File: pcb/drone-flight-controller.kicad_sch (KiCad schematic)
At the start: 88 parts, among them J1 SWD, J10 CONN_MANDO, J11 OLED, J12 STM32 SPI, J13 STM32 I2C, J14 STM32 USART, J2 Jumper, J3 USB_B_Micro, J4 CONN_MOT_1, J5 CONN_MOT_2, J6 CONN_MOT_3, J7 CONN_MOT_4, J8 XT-60, J9 LIDAR, SW1 TS24CA_C393942, SW2 TS24CA_C393942, SW4 SW_Push_SPDT, U1 STM32F103R8T6, U10 LM7805_TO220, U11 AMS1117-3.3, U2 MPU-6050, Y1 8MHz, Y2 32.768KHz

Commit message: pcb: switch SW1-SW3 to the TC-6610 THT tact switch (C7528713)
Replace the low-profile side-actuated TS24CA with a tall 9mm 6x6 THT
button that stays reachable on the assembled frame. The 4-pin part has
internally shorted pin pairs across its 6.5mm axis, so the distinct
1/2/3/4 pad numbering of the converted EasyEDA footprint would strap
each net across a shorted pair (STM32 held in reset); use KiCad's
official SW_PUSH_6mm_H9.5mm instead, whose paired 1,1,2,2 pads encode
the topology and drop onto the existing 2-pin symbols. Headless KiCad
10 ERC is identical before and after.
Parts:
- SW1, SW2: value TS24CA_C393942 -> TC-6610_C7528713; footprint easyeda:SW-SMD_2P-TS24CA -> Button_Switch_THT:SW_PUSH_6mm_H9.5mm; LCSC C393942 -> C7528713; Manufacturer SHOU HAN -> FG; Part TS24CA -> TC-6610 -6*6*9-260g
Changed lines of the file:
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@@
 			)
 		)
-		(property "Value" "TS24CA_C393942"
+		(property "Value" "TC-6610_C7528713"
 			(at 385.064 162.56 90)
 			(hide yes)
@@
 			)
 		)
-		(property "Footprint" "easyeda:SW-SMD_2P-TS24CA"
+		(property "Footprint" "Button_Switch_THT:SW_PUSH_6mm_H9.5mm"
 			(at 387.35 161.29 0)
 			(hide yes)
@@
 			)
 		)
-		(property "Datasheet" "https://www.lcsc.com/datasheet/lcsc_datasheet_2404241539_SHOU-HAN-TS24CA_C393942.pdf"
+		(property "Datasheet" "https://wmsc.lcsc.com/wmsc/upload/file/pdf/v2/lcsc/2401191746_FG-TC-6610--6-6-9-260g_C7528713.pdf"
 			(at 387.35 161.29 0)
 			(hide yes)
@@
 			)
 		)
-		(property "Description" "Push button switch, generic, two pins"
+		(property "Description" "-20℃~+70℃ 12V 2.6N 50,000 cycles 50mA 6mm 6mm Black Round Button SPST Through Hole Without Bracket 插件-4P,6x6mm Tactile Switches ROHS"
 			(at 382.27 161.29 0)
 			(hide yes)
@@
 			)
 		)
-		(property "LCSC" "C393942"
+		(property "LCSC" "C7528713"
 			(at 382.27 161.29 0)
 			(hide yes)
@@
 			)
 		)
-		(property "Part" "TS24CA"
+		(property "Part" "TC-6610 -6*6*9-260g"
 			(at 382.27 161.29 0)
 			(hide yes)
@@
 			)
 		)
-		(property "Manufacturer" "SHOU HAN"
+		(property "Manufacturer" "FG"
 			(at 382.27 161.29 0)
 			(hide yes)
@@
 			)
 		)
-		(property "Value" "TS24CA_C393942"
+		(property "Value" "TC-6610_C7528713"
 			(at 25.4 199.3899 90)
 			(hide yes)
@@
 			)
 		)
-		(property "Footprint" "easyeda:SW-SMD_2P-TS24CA"
+		(property "Footprint" "Button_Switch_THT:SW_PUSH_6mm_H9.5mm"
 			(at 26.67 198.12 0)
 			(hide yes)
@@
 			)
 		)
-		(property "Datasheet" "https://www.lcsc.com/datasheet/lcsc_datasheet_2404241539_SHOU-HAN-TS24CA_C393942.pdf"
+		(property "Datasheet" "https://wmsc.lcsc.com/wmsc/upload/file/pdf/v2/lcsc/2401191746_FG-TC-6610--6-6-9-260g_C7528713.pdf"
 			(at 26.67 198.12 0)
 			(hide yes)
@@
 			)
 		)
-		(property "Description" "Push button switch, generic, two pins"
+		(property "Description" "-20℃~+70℃ 12V 2.6N 50,000 cycles 50mA 6mm 6mm Black Round Button SPST Through Hole Without Bracket 插件-4P,6x6mm Tactile Switches ROHS"
 			(at 21.59 198.12 0)
 			(hide yes)
@@
 			)
 		)
-		(property "LCSC" "C393942"
+		(property "LCSC" "C7528713"
 			(at 21.59 198.12 0)
 			(hide yes)
@@
 			)
 		)
-		(property "Part" "TS24CA"
+		(property "Part" "TC-6610 -6*6*9-260g"
 			(at 21.59 198.12 0)
 			(hide yes)
@@
 			)
 		)
-		(property "Manufacturer" "SHOU HAN"
+		(property "Manufacturer" "FG"
 			(at 21.59 198.12 0)
 			(hide yes)

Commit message: pcb: 3D models for U3, U5, J3, J16
U3 and U5 move from the model-less DigiKey footprints to the official
KiCad TQFP-32 and SOIC-8 footprints, whose STEP models ship with the
AppImage. J3/J16's micro-USB footprint had no model, no MPN, and
unknown provenance - replaced wholesale with the SHOU HAN MicroXNJ
(C404969): converted footprint with shell legs renumbered to the
Shield pin 6, STEP model, and BOM fields, verified against its
datasheet drawing. ERC caught that the LM358 is multi-unit and the
first edit only touched U5A's footprint field; U5B fixed to match.
Headless KiCad 10 ERC identical to baseline.
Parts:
- J3: footprint easyeda:MICRO-USB-SMD_5P-P0.65-H-F_MICRO5.9MMUSB -> easyeda:MICRO-USB-SMD_MICROXNJ_1; LCSC (none) -> C404969; Manufacturer (none) -> SHOU HAN; Part (none) -> MicroXNJ
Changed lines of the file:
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@@
 			)
 		)
-		(property "Footprint" "easyeda:MICRO-USB-SMD_5P-P0.65-H-F_MICRO5.9MMUSB"
+		(property "Footprint" "easyeda:MICRO-USB-SMD_MICROXNJ_1"
 			(at 106.68 267.97 0)
 			(hide yes)
@@
 			)
 		)
-		(property "Datasheet" ""
+		(property "Datasheet" "https://www.lcsc.com/datasheet/lcsc_datasheet_2204151400_SHOU-HAN-MicroXNJ_C404969.pdf"
 			(at 106.68 267.97 0)
 			(hide yes)
@@
 			)
 		)
-		(property "Description" "USB Micro Type B connector"
+		(property "Description" "-20℃~+85℃ 1 1.8A 30V 5,000 times 5P Black Female Micro-B Surface Mount, Right Angle USB 2.0 SMD USB Connectors ROHS"
 			(at 110.49 269.24 0)
 			(hide yes)
@@
 			)
 		)
+    (property "LCSC" "C404969" (at 110.49 269.24 0)
+      (effects (font (size 1.27 1.27)) (hide yes))
+    )
+    (property "Part" "MicroXNJ" (at 110.49 269.24 0)
+      (effects (font (size 1.27 1.27)) (hide yes))
+    )
+    (property "Manufacturer" "SHOU HAN" (at 110.49 269.24 0)
+      (effects (font (size 1.27 1.27)) (hide yes))
+    )
 		(pin "3"
 		)

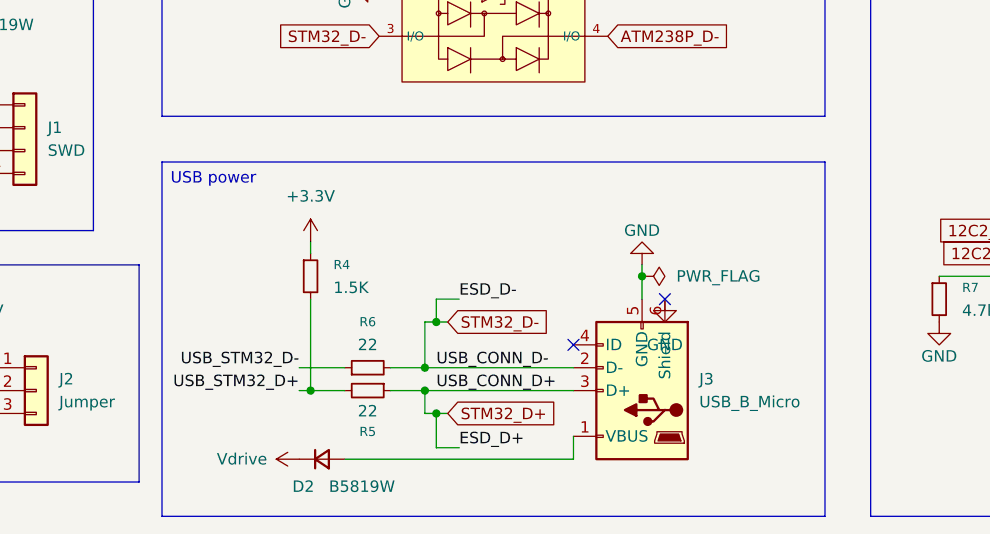
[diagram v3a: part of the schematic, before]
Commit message: pcb: import the new U3/U5/USB footprints onto the board
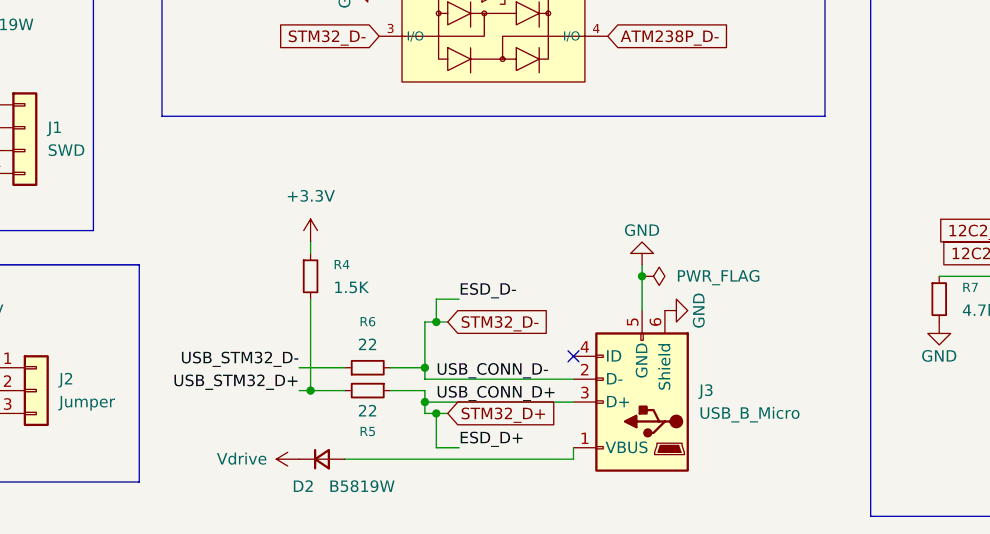
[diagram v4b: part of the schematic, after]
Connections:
- no-connect marks 22 -> 21
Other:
- moved on the sheet: J3
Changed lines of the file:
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@@
 		)
 	)
-	(text_box "USB power\n"
-		(exclude_from_sim no)
-		(at 57.15 243.84 0)
-		(size 73.66 39.37)
-		(margins 0.9525 0.9525 0.9525 0.9525)
-		(stroke
-			(width 0)
-			(type solid)
-		)
-		(fill
-			(type none)
-		)
-		(effects
-			(font
-				(size 1.27 1.27)
-			)
-			(justify left top)
-		)
-	)
 	(text_box "Reset button\n"
 		(exclude_from_sim no)
@@
 	)
 	(junction
-		(at 86.36 266.7)
-		(diameter 0)
-		(color 0 0 0 0)
-	)
-	(junction
-		(at 110.49 256.54)
-		(diameter 0)
-		(color 0 0 0 0)
-	)
-	(junction
 		(at 260.35 234.95)
 		(diameter 0)
@@
 	)
 	(junction
+		(at 86.36 266.7)
+		(diameter 0)
+		(color 0 0 0 0)
+	)
+	(junction
 		(at 161.29 170.18)
 		(diameter 0)
@@
 	)
 	(junction
+		(at 86.36 270.51)
+		(diameter 0)
+		(color 0 0 0 0)
+	)
+	(junction
 		(at 48.26 67.31)
 		(diameter 0)
@@
 	)
 	(junction
+		(at 110.49 256.54)
+		(diameter 0)
+		(color 0 0 0 0)
+	)
+	(junction
 		(at 87.63 271.78)
 		(diameter 0)
@@
 		(color 0 0 0 0)
 	)
-	(junction
-		(at 86.36 269.24)
-		(diameter 0)
-		(color 0 0 0 0)
-	)
 	(no_connect
 		(at 219.71 102.87)
@@
 	)
 	(no_connect
-		(at 102.87 264.16)
+		(at 102.87 265.43)
 	)
 	(no_connect
@@
 	)
 	(no_connect
-		(at 113.03 259.08)
-	)
-	(no_connect
 		(at 184.15 118.11)
 	)
@@
 	(wire
 		(pts
-			(xy 86.36 271.78) (xy 86.36 269.24)
+			(xy 86.36 271.78) (xy 86.36 270.51)
 		)
 		(stroke
@@
 	(wire
 		(pts
-			(xy 86.36 269.24) (xy 102.87 269.24)
+			(xy 86.36 270.51) (xy 102.87 270.51)
 		)
 		(stroke
@@
 	(wire
 		(pts
-			(xy 102.87 274.32) (xy 102.87 276.86)
+			(xy 102.87 275.59) (xy 102.87 276.86)
 		)
 		(stroke
@@
 	(wire
 		(pts
-			(xy 86.36 266.7) (xy 102.87 266.7)
+			(xy 86.36 267.97) (xy 102.87 267.97)
 		)
 		(stroke
@@
 	(wire
 		(pts
-			(xy 110.49 256.54) (xy 110.49 259.08)
+			(xy 86.36 270.51) (xy 86.36 269.24)
 		)
 		(stroke
@@
 	(wire
 		(pts
+			(xy 86.36 267.97) (xy 86.36 266.7)
+		)
+		(stroke
+			(width 0)
+			(type default)
+		)
+	)
+	(wire
+		(pts
 			(xy 177.8 21.59) (xy 177.8 24.13)
 		)
@@
 	(wire
 		(pts
+			(xy 110.49 256.54) (xy 110.49 260.35)
+		)
+		(stroke
+			(width 0)
+			(type default)
+		)
+	)
+	(wire
+		(pts
 			(xy 88.9 261.62) (xy 87.63 261.62)
 		)
@@
 	)
 	(label "USB_CONN_D-"
-		(at 87.63 266.7 0)
+		(at 87.63 267.97 0)
 		(effects
 			(font
@@
 	)
 	(label "USB_CONN_D+"
-		(at 87.63 269.24 0)
+		(at 87.63 270.51 0)
 		(effects
 			(font
@@
 	)
 	(symbol
+		(lib_id "PCM_SparkFun-PowerSymbol:GND")
+		(at 113.03 260.35 90)
+		(unit 1)
+		(body_style 1)
+		(exclude_from_sim no)
+		(in_bom yes)
+		(on_board yes)
+		(in_pos_files yes)
+		(dnp no)
+		(fields_autoplaced yes)
+		(property "Reference" "#PWR078"
+			(at 119.38 260.35 0)
+			(hide yes)
+			(show_name no)
+			(do_not_autoplace no)
+			(effects
+				(font
+					(size 1.27 1.27)
+				)
+			)
+		)
+		(property "Value" "GND"
+			(at 116.84 260.35 0)
+			(show_name no)
+			(do_not_autoplace yes)
+			(effects
+				(font
+					(size 1.27 1.27)
+				)
+			)
+		)
+		(property "Footprint" ""
+			(at 113.03 260.35 0)
+			(hide yes)
+			(show_name no)
+			(do_not_autoplace no)
+			(effects
+				(font
+					(size 1.27 1.27)
+				)
+			)
+		)
+		(property "Datasheet" ""
+			(at 113.03 260.35 0)
+			(hide yes)
+			(show_name no)
+			(do_not_autoplace no)
+			(effects
+				(font
+					(size 1.27 1.27)
+				)
+			)
+		)
+		(property "Description" "Power symbol creates a global label with name \"GND\" , ground"
+			(at 121.92 260.35 0)
+			(hide yes)
+			(show_name no)
+			(do_not_autoplace no)
+			(effects
+				(font
+					(size 1.27 1.27)
+				)
+			)
+		)
+		(pin "1"
+		)
+		(instances
+			(project "drone-flight-controller"
+				(path "/2753c1d5-c5b3-42f6-8923-cca974813b6b"
+					(reference "#PWR078")
+					(unit 1)
+				)
+			)
+		)
+	)
+	(symbol
 		(lib_id "Mechanical:MountingHole_Pad")
 		(at 271.78 232.41 0)
@@
 	(symbol
 		(lib_id "Connector:USB_B_Micro")
-		(at 110.49 269.24 180)
+		(at 110.49 270.51 180)
 		(unit 1)
 		(body_style 1)
@@
 		(fields_autoplaced yes)
 		(property "Reference" "J3"
-			(at 116.84 267.9699 0)
+			(at 116.84 269.2399 0)
 			(show_name no)
 			(do_not_autoplace no)
@@
 		)
 		(property "Value" "USB_B_Micro"
-			(at 116.84 270.5099 0)
+			(at 116.84 271.7799 0)
 			(show_name no)
 			(do_not_autoplace no)
@@
 		)
 		(property "Footprint" "easyeda:MICRO-USB-SMD_MICROXNJ_1"
-			(at 106.68 267.97 0)
+			(at 106.68 269.24 0)
 			(hide yes)
 			(show_name no)
@@
 		)
 		(property "Datasheet" "https://www.lcsc.com/datasheet/lcsc_datasheet_2204151400_SHOU-HAN-MicroXNJ_C404969.pdf"
-			(at 106.68 267.97 0)
+			(at 106.68 269.24 0)
 			(hide yes)
 			(show_name no)
@@
 		)
 		(property "Description" "-20℃~+85℃ 1 1.8A 30V 5,000 times 5P Black Female Micro-B Surface Mount, Right Angle USB 2.0 SMD USB Connectors ROHS"
-			(at 110.49 269.24 0)
+			(at 110.49 270.51 0)
+			(hide yes)
+			(show_name no)
+			(do_not_autoplace no)
+			(effects
+				(font
+					(size 1.27 1.27)
+				)
+			)
+		)
+		(property "LCSC" "C404969"
+			(at 110.49 270.51 0)
+			(hide yes)
+			(show_name no)
+			(do_not_autoplace no)
+			(effects
+				(font
+					(size 1.27 1.27)
+				)
+			)
+		)
+		(property "Part" "MicroXNJ"
+			(at 110.49 270.51 0)
+			(hide yes)
+			(show_name no)
+			(do_not_autoplace no)
+			(effects
+				(font
+					(size 1.27 1.27)
+				)
+			)
+		)
+		(property "Manufacturer" "SHOU HAN"
+			(at 110.49 270.51 0)
 			(hide yes)
 			(show_name no)
@@
 			)
 		)
-    (property "LCSC" "C404969" (at 110.49 269.24 0)
-      (effects (font (size 1.27 1.27)) (hide yes))
-    )
-    (property "Part" "MicroXNJ" (at 110.49 269.24 0)
-      (effects (font (size 1.27 1.27)) (hide yes))
-    )
-    (property "Manufacturer" "SHOU HAN" (at 110.49 269.24 0)
-      (effects (font (size 1.27 1.27)) (hide yes))
-    )
 		(pin "3"
 		)
@@
 					(unit 1)
 				)
-			)
-		)
-	)
-	(symbol
-		(lib_id "power:GND")
-		(at 113.03 259.08 0)
-		(unit 1)
-		(body_style 1)
-		(exclude_from_sim no)
-		(in_bom yes)
-		(on_board yes)
-		(in_pos_files yes)
-		(dnp no)
-		(fields_autoplaced yes)
-		(property "Reference" "#PWR0142"
-			(at 113.03 265.43 0)
-			(hide yes)
-			(show_name no)
-			(do_not_autoplace no)
-			(effects
-				(font
-					(size 1.27 1.27)
-				)
-			)
-		)
-		(property "Value" "GND"
-			(at 113.03 264.16 0)
-			(show_name no)
-			(do_not_autoplace no)
-			(effects
-				(font
-					(size 1.27 1.27)
-				)
-			)
-		)
-		(property "Footprint" ""
-			(at 113.03 259.08 0)
-			(hide yes)
-			(show_name no)
-			(do_not_autoplace no)
-			(effects
-				(font
-					(size 1.27 1.27)
-				)
-			)
-		)
-		(property "Datasheet" ""
-			(at 113.03 259.08 0)
-			(hide yes)
-			(show_name no)
-			(do_not_autoplace no)
-			(effects
-				(font
-					(size 1.27 1.27)
-				)
-			)
-		)
-		(property "Description" "Power symbol creates a global label with name GND, ground"
-			(at 113.03 259.08 0)
-			(hide yes)
-			(show_name no)
-			(do_not_autoplace no)
-			(effects
-				(font
-					(size 1.27 1.27)
-				)
-			)
-		)
-		(pin "1"
-		)
-		(instances
-			(project "drone-flight-controller"
-				(path "/2753c1d5-c5b3-42f6-8923-cca974813b6b"
-					(reference "#PWR0142")
-					(unit 1)
-				)

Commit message: pcb: session state - U10 folded on board, pending sch fixes
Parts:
- U10: footprint Package_TO_SOT_THT:TO-220-3_Vertical -> Package_TO_SOT_THT:TO-220-3_Horizontal_TabDown
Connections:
- net +3.3V: now also J9.2 (Pin_2); no longer J9.5 (Pin_5)
- net +5V: now also J14.4 (Pin_4), J9.6 (Pin_6); no longer J14.1 (Pin_1), J9.1 (Pin_1)
- net GND: now also J14.1 (Pin_1), J3.SH (Shield), J9.3 (Pin_3); no longer J14.4 (Pin_4), J3.6 (Shield), J9.4 (Pin_4)
- net ON_OFF_LIDAR: now also J9.1 (Pin_1); no longer J9.6 (Pin_6)
- net USART1_RX: now also J14.3 (Pin_3), J9.4 (Pin_4); no longer J14.2 (Pin_2), J9.3 (Pin_3)
- net USART1_TX: now also J14.2 (Pin_2), J9.5 (Pin_5); no longer J14.3 (Pin_3), J9.2 (Pin_2)
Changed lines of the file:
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@@
 		)
 	)
+	(text_box "Power\n"
+		(exclude_from_sim no)
+		(at 57.15 245.11 0)
+		(size 72.39 39.37)
+		(margins 0.9525 0.9525 0.9525 0.9525)
+		(stroke
+			(width 0)
+			(type solid)
+		)
+		(fill
+			(type none)
+		)
+		(effects
+			(font
+				(size 1.27 1.27)
+			)
+			(justify left top)
+		)
+	)
 	(text_box "Programming\n"
 		(exclude_from_sim no)
@@
 	(wire
 		(pts
-			(xy 313.69 241.3) (xy 325.12 241.3)
-		)
-		(stroke
-			(width 0)
-			(type default)
-		)
-	)
-	(wire
-		(pts
 			(xy 210.82 29.21) (xy 210.82 31.75)
 		)
@@
 	(wire
 		(pts
+			(xy 313.69 241.3) (xy 325.12 241.3)
+		)
+		(stroke
+			(width 0)
+			(type default)
+		)
+	)
+	(wire
+		(pts
 			(xy 187.96 29.21) (xy 187.96 31.75)
 		)
@@
 	(wire
 		(pts
-			(xy 307.34 238.76) (xy 325.12 238.76)
-		)
-		(stroke
-			(width 0)
-			(type default)
-		)
-	)
-	(wire
-		(pts
 			(xy 271.78 234.95) (xy 260.35 234.95)
 		)
@@
 	(wire
 		(pts
+			(xy 307.34 238.76) (xy 325.12 238.76)
+		)
+		(stroke
+			(width 0)
+			(type default)
+		)
+	)
+	(wire
+		(pts
 			(xy 86.36 261.62) (xy 86.36 266.7)
 		)
@@
 			)
 		)
-		(property "Description" "-20℃~+70℃ 12V 2.6N 50,000 cycles 50mA 6mm 6mm Black Round Button SPST Through Hole Without Bracket 插件-4P,6x6mm Tactile Switches ROHS"
+		(property "Description" "Push button switch, generic, two pins"
 			(at 382.27 161.29 0)
 			(hide yes)
@@
 	(symbol
 		(lib_id "Connector_Generic:Conn_01x06")
-		(at 330.2 236.22 0)
+		(at 330.2 238.76 0)
+		(mirror x)
 		(unit 1)
 		(body_style 1)
@@
 		(in_pos_files yes)
 		(dnp no)
-		(fields_autoplaced yes)
 		(property "Reference" "J9"
-			(at 332.74 236.2199 0)
+			(at 332.74 238.7601 0)
 			(show_name no)
 			(do_not_autoplace no)
@@
 		)
 		(property "Value" "LIDAR"
-			(at 332.74 238.7599 0)
+			(at 332.74 236.2201 0)
 			(show_name no)
 			(do_not_autoplace no)
@@
 		)
 		(property "Footprint" "Connector_PinHeader_2.54mm:PinHeader_1x06_P2.54mm_Horizontal"
-			(at 330.2 236.22 0)
+			(at 330.2 238.76 0)
 			(hide yes)
 			(show_name no)
@@
 		)
 		(property "Datasheet" ""
-			(at 330.2 236.22 0)
+			(at 330.2 238.76 0)
 			(hide yes)
 			(show_name no)
@@
 		)
 		(property "Description" "Generic connector, single row, 01x06, script generated (kicad-library-utils/schlib/autogen/connector/)"
-			(at 330.2 236.22 0)
+			(at 330.2 238.76 0)
 			(hide yes)
 			(show_name no)
@@
 			)
 		)
-		(property "Description" "-20℃~+85℃ 1 1.8A 30V 5,000 times 5P Black Female Micro-B Surface Mount, Right Angle USB 2.0 SMD USB Connectors ROHS"
+		(property "Description" "USB Micro Type B connector"
 			(at 110.49 270.51 0)
 			(hide yes)
@@
 		(pin "1"
 		)
-		(pin "6"
+		(pin "SH"
 		)
 		(pin "4"
@@
 			)
 		)
-		(property "Footprint" "Package_TO_SOT_THT:TO-220-3_Vertical"
+		(property "Footprint" "Package_TO_SOT_THT:TO-220-3_Horizontal_TabDown"
 			(at 59.69 61.595 0)
 			(hide yes)
@@
 			)
 		)
-		(property "Description" "-20℃~+70℃ 12V 2.6N 50,000 cycles 50mA 6mm 6mm Black Round Button SPST Through Hole Without Bracket 插件-4P,6x6mm Tactile Switches ROHS"
+		(property "Description" "Push button switch, generic, two pins"
 			(at 21.59 198.12 0)
 			(hide yes)
@@
 	(symbol
 		(lib_id "Connector_Generic:Conn_01x04")
-		(at 350.52 26.67 0)
+		(at 350.52 29.21 0)
+		(mirror x)
 		(unit 1)
 		(body_style 1)
@@
 		(in_pos_files yes)
 		(dnp no)
-		(fields_autoplaced yes)
 		(property "Reference" "J14"
-			(at 353.06 26.6699 0)
+			(at 353.06 29.2101 0)
 			(show_name no)
 			(do_not_autoplace no)
@@
 		)
 		(property "Value" "STM32 USART"
-			(at 353.06 29.2099 0)
+			(at 353.06 26.6701 0)
 			(show_name no)
 			(do_not_autoplace no)
@@
 		)
 		(property "Footprint" "Connector_PinHeader_2.54mm:PinHeader_1x04_P2.54mm_Horizontal"
-			(at 350.52 26.67 0)
+			(at 350.52 29.21 0)
 			(hide yes)
 			(show_name no)
@@
 		)
 		(property "Datasheet" ""
-			(at 350.52 26.67 0)
+			(at 350.52 29.21 0)
 			(hide yes)
 			(show_name no)
@@
 		)
 		(property "Description" "Generic connector, single row, 01x04, script generated (kicad-library-utils/schlib/autogen/connector/)"
-			(at 350.52 26.67 0)
+			(at 350.52 29.21 0)
 			(hide yes)
 			(show_name no)

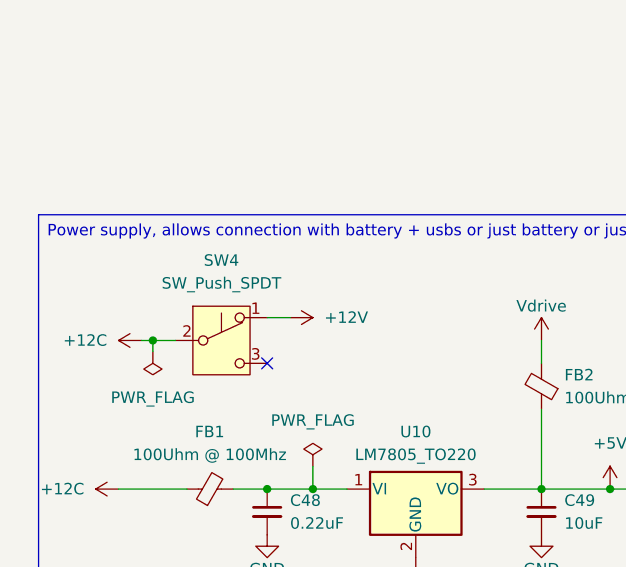
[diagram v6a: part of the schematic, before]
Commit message: pcb: source SW4 as the SS12D10G5 slide switch (C7431054)
Retire the last named unsourced part: the master power switch becomes
a real latching SPDT slide rated 2A/125V - about 5x margin over the
logic tree's draw through the LM7805 branch. The converted footprint's
middle pad is the SPDT common, matching the existing +12V/+12C wiring
with no renumbering, and it brings the 3D model the placeholder
Switch_Slide footprint never had. Headless ERC identical.
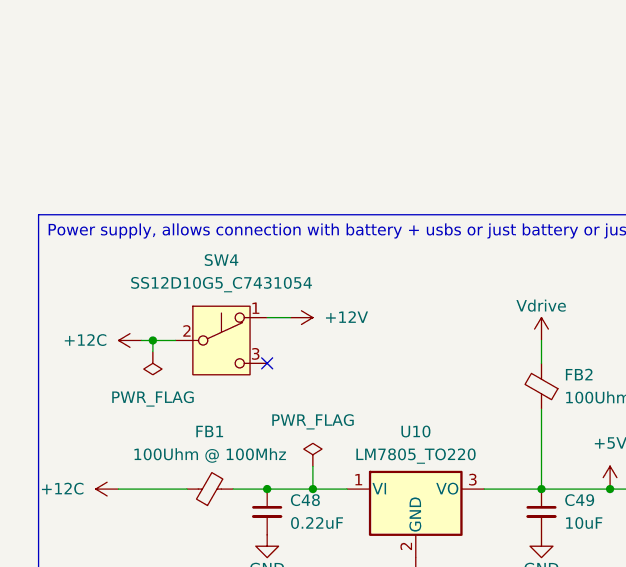
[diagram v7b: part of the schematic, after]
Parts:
- SW4: value SW_Push_SPDT -> SS12D10G5_C7431054; footprint easyeda:Switch_Slide -> easyeda:SW-TH_SHOU-HAN_SS12D10G4; LCSC (none) -> C7431054; Manufacturer (none) -> SHOU HAN; Part (none) -> SS12D10G5
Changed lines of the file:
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@@
 			)
 		)
-		(property "Value" "SW_Push_SPDT"
+		(property "Value" "SS12D10G5_C7431054"
 			(at 38.1 44.45 0)
 			(show_name no)
@@
 			)
 		)
-		(property "Footprint" "easyeda:Switch_Slide"
+		(property "Footprint" "easyeda:SW-TH_SHOU-HAN_SS12D10G4"
 			(at 38.1 50.8 0)
 			(hide yes)
@@
 			)
 		)
-		(property "Datasheet" ""
+		(property "Datasheet" "https://wmsc.lcsc.com/wmsc/upload/file/pdf/v2/lcsc/2311301507_SHOU-HAN-SS12D10G5_C7431054.pdf"
 			(at 38.1 50.8 0)
 			(hide yes)
@@
 			)
 		)
-		(property "Description" "Momentary Switch, single pole double throw"
+		(property "Description" "-25℃~+70℃ 12.7mm 125V 2A 3,000 Cycles 6.7mm SPDT Through Hole 插件,12.7x6.7mm Slide Switches ROHS"
 			(at 38.1 50.8 0)
 			(hide yes)
@@
 			)
 		)
+    (property "LCSC" "C7431054" (at 38.1 50.8 0)
+      (effects (font (size 1.27 1.27)) (hide yes))
+    )
+    (property "Part" "SS12D10G5" (at 38.1 50.8 0)
+      (effects (font (size 1.27 1.27)) (hide yes))
+    )
+    (property "Manufacturer" "SHOU HAN" (at 38.1 50.8 0)
+      (effects (font (size 1.27 1.27)) (hide yes))
+    )
 		(pin "1"
 		)
